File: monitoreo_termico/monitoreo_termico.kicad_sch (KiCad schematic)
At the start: 9 parts, among them U1 LM358, U2 LM358, U3 LM35-D, U4 LM358

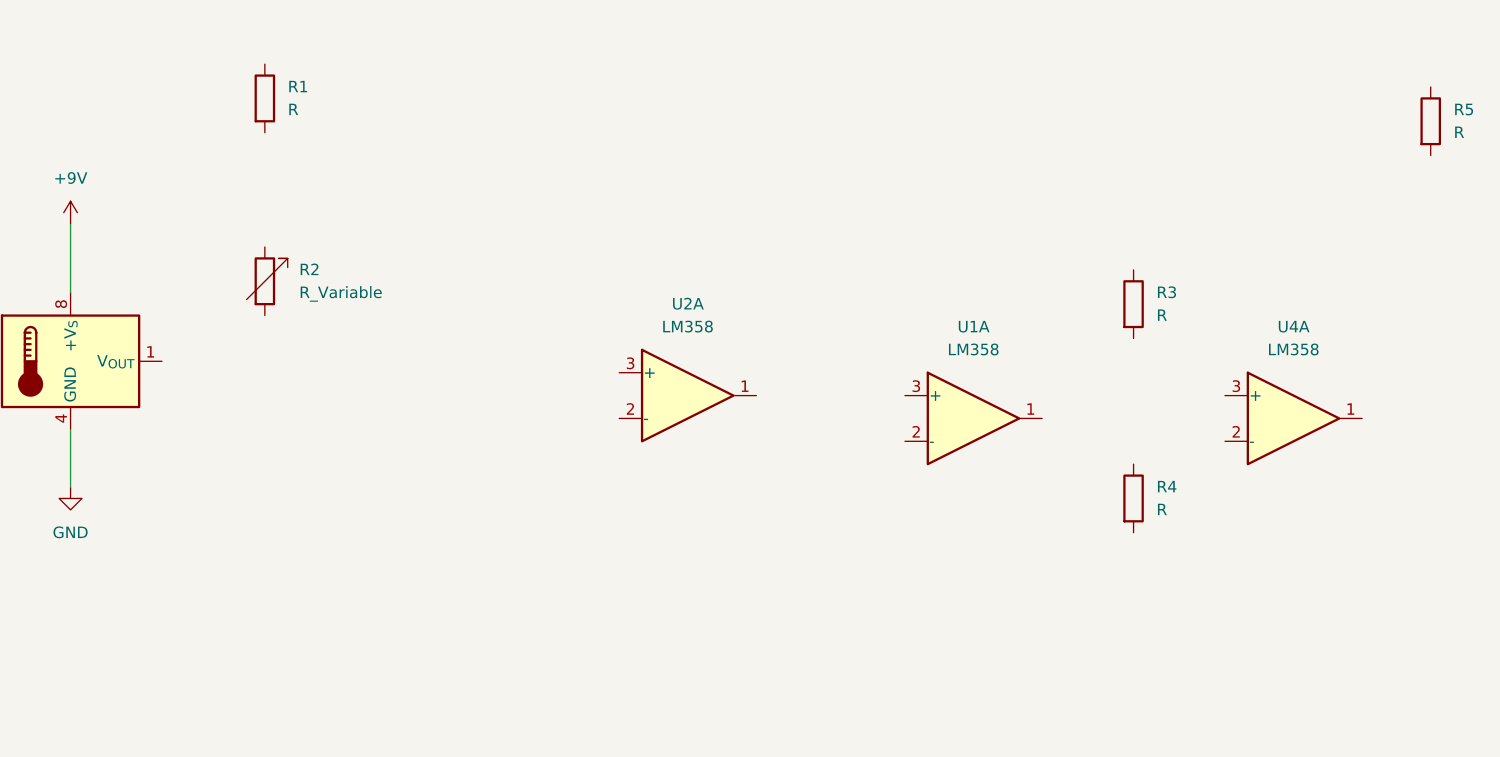
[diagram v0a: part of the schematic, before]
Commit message: Agregué el esquemático del TP1
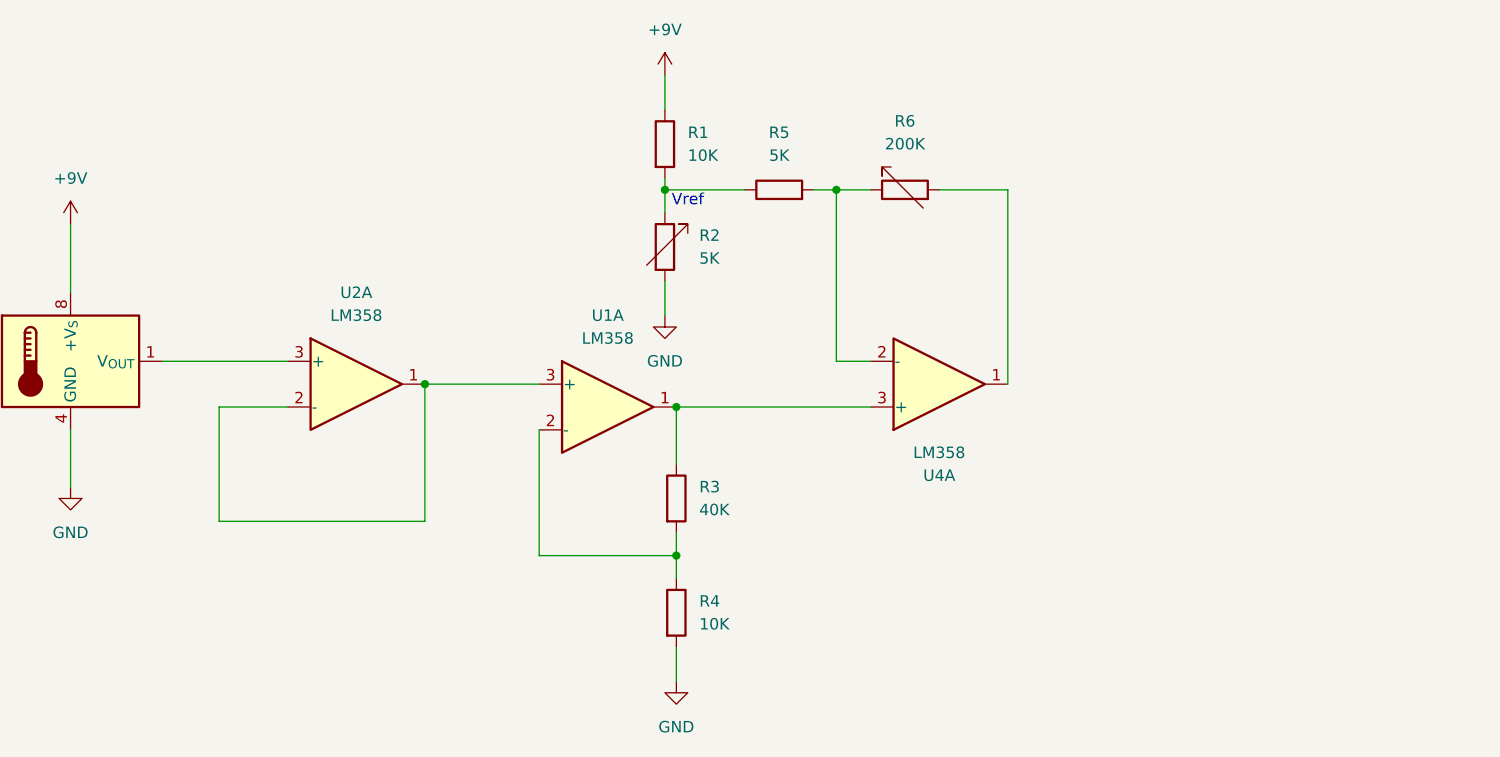
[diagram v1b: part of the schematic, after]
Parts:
- added R6: 200K, symbol Device:R_Variable
- R1, R4: value R -> 10K
- R2: value R_Variable -> 5K
- R3: value R -> 40K
- R5: value R -> 5K
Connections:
- net +9V: now also R1.1
- net GND: now also R2.2, R4.2
- net at U4.1: now also R6.2
- net at U4.2 (-): now also R5.2, R6.1
- net at U4.3 (+): now also R3.1, U1.1
- net at U2.1: now also U1.3 (+), U2.2 (-)
- net at U2.3 (+): now also U3.1 (V_{OUT})
- net at R4.1: now also R3.2, U1.2 (-)
- net at R1.2: now also R2.1, R5.1
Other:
- note added: "Vref"
- moved on the sheet: R1, R2, R3, R4, U1A, U2A, U4A

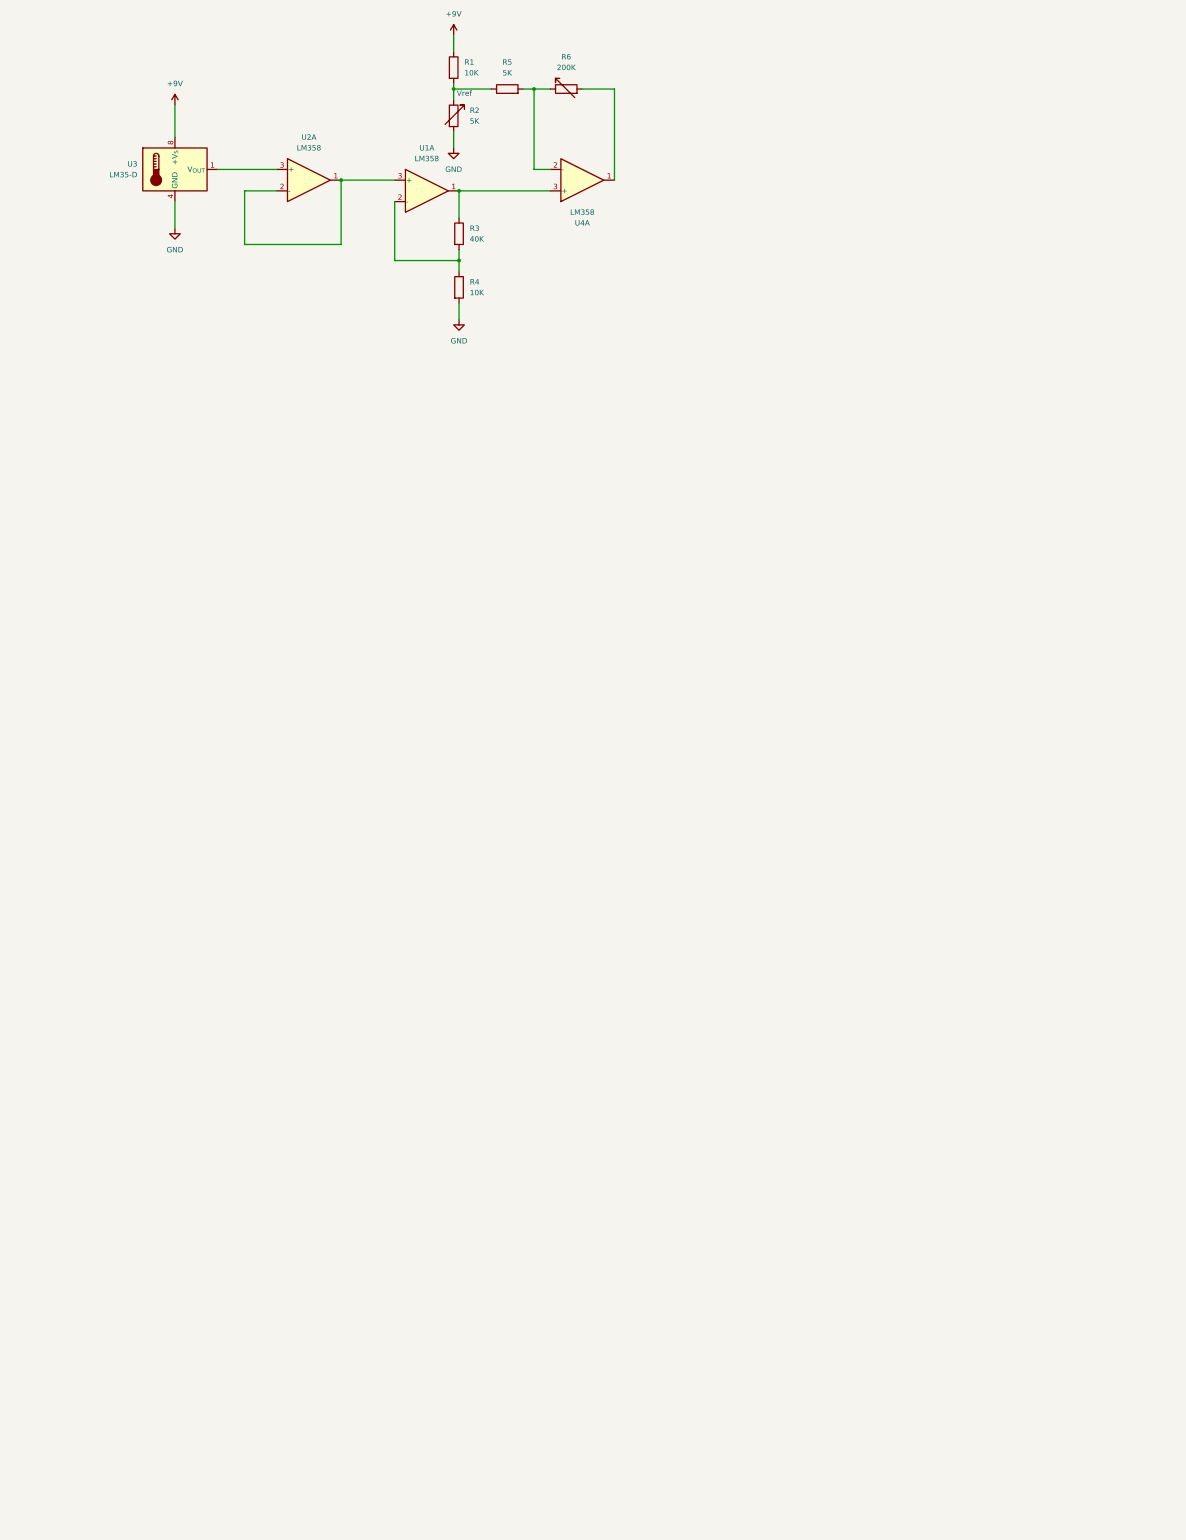
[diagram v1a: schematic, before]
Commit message: agregue el esquematico en kicad del lab 8
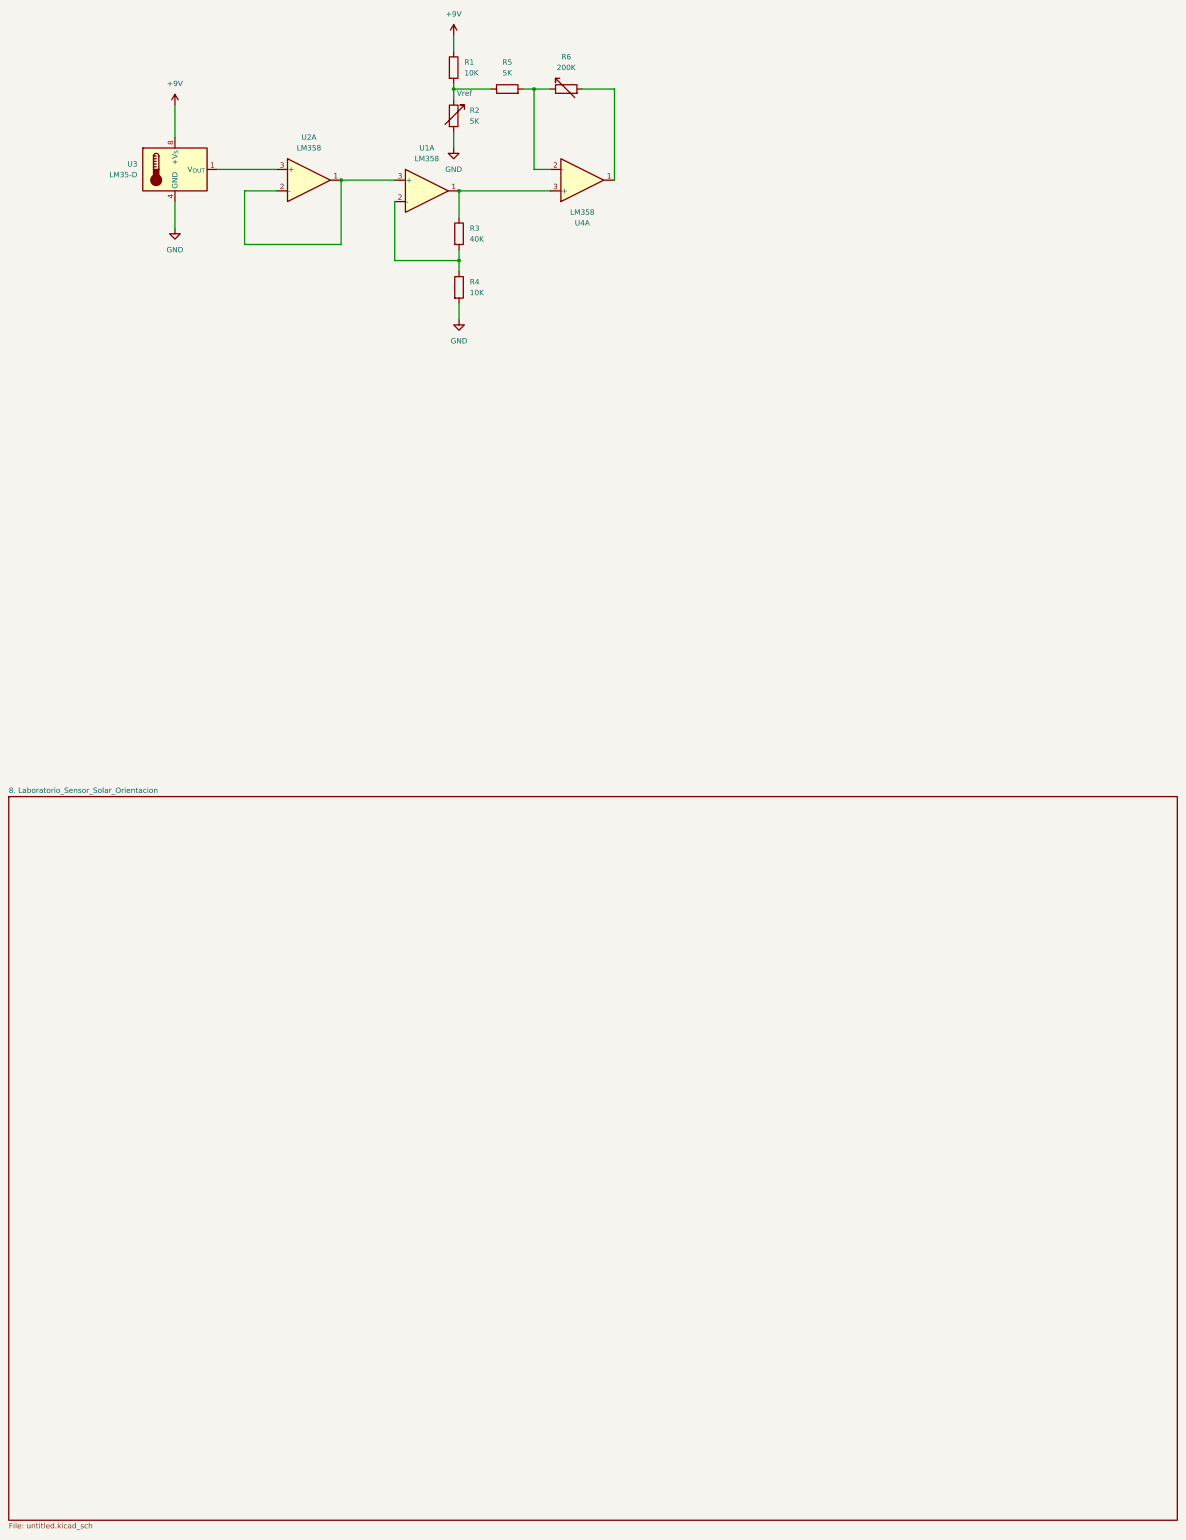
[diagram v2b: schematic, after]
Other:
- added sheet 8. Laboratorio_Sensor_Solar_Orientacion (untitled.kicad_sch)
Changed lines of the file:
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@@
+		)
+	)
+	(sheet
+		(at 10.16 224.79)
+		(size 276.86 171.45)
+		(exclude_from_sim no)
+		(in_bom yes)
+		(on_board yes)
+		(dnp no)
+		(fields_autoplaced yes)
+		(stroke
+			(width 0.1524)
+			(type solid)
+		)
+		(fill
+			(color 0 0 0 0.0000)
+		)
+		(property "Sheetname" "8. Laboratorio_Sensor_Solar_Orientacion"
+			(at 10.16 224.0784 0)
+			(effects
+				(font
+					(size 1.27 1.27)
+				)
+				(justify left bottom)
+			)
+		)
+		(property "Sheetfile" "untitled.kicad_sch"
+			(at 10.16 396.8246 0)
+			(effects
+				(font
+					(size 1.27 1.27)
+				)
+				(justify left top)
+			)
+		)
+		(instances
+			(project "monitoreo_termico"
+				(path "/a0aa5472-87de-4e10-861a-104b546c9985"
+					(page "2")
+				)
+			)
 		)
 	)
